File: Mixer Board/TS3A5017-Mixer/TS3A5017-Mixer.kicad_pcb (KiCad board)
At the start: 2 copper layers, 37.8 x 42.9 mm, 10 parts, among them J1 RF-In, J2 CLK0, J3 CLK1, J4 Conn_01x06, U1 TS3A5017RGY

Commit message: Working on mixer board
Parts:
- added C10: .1uf, Capacitor_SMD:C_0201_0603Metric, F.Cu at (107.9, 68.1)
- added C11: .1uf, Capacitor_SMD:C_0201_0603Metric, F.Cu at (110.4, 61.1)
- added C12: .1uf, Capacitor_SMD:C_0201_0603Metric, F.Cu at (110.4, 62.8)
- added C13: .1uf, Capacitor_SMD:C_0201_0603Metric, F.Cu at (110.4, 64.6)
- added C6: .1uf, Capacitor_SMD:C_0201_0603Metric, F.Cu at (107.9, 61.1)
- added C7: .1uf, Capacitor_SMD:C_0201_0603Metric, F.Cu at (107.9, 62.8)
- added C8: .1uf, Capacitor_SMD:C_0201_0603Metric, F.Cu at (107.9, 64.6)
- added C9: .1uf, Capacitor_SMD:C_0201_0603Metric, F.Cu at (107.9, 66.3)
- added R1: 10k, Resistor_SMD:R_0201_0603Metric, F.Cu at (110.4, 66.3)
- added R2: 10k, Resistor_SMD:R_0201_0603Metric, F.Cu at (110.4, 68.1)
- added U2: LMP7715MF, Package_TO_SOT_SMD:SOT-23-5, F.Cu at (109.3, 53.3)
- added U3: LMP7715MF, Package_TO_SOT_SMD:SOT-23-5, F.Cu at (109.3, 58.0)
- J1, J2, J3: footprint Connector_Amphenol:AMPHENOL_901-143-6RFX -> Connector_Coaxial:SMA_Amphenol_901-143_Horizontal
- J4: value Conn_01x06 -> AudioJack4_Ground; footprint Connector_PinHeader_2.54mm:PinHeader_1x06_P2.54mm_Vertical -> Connector_Audio:Jack_3.5mm_CUI_SJ-3523-SMT_Horizontal
- moved J4 56.0 mm to (135.0, 51.4), turned to 0 degrees
- turned J1 to 0 degrees
- turned J2 to -90 degrees
- turned J3 to 90 degrees
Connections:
- C2 pad 1: Net-(J4-Pin_5) -> Net-(U1-1S4)
- C3 pad 1: Net-(J4-Pin_4) -> Net-(U1-1S3)
- C4 pad 1: Net-(J4-Pin_3) -> Net-(U1-1S2)
- C5 pad 1: Net-(J4-Pin_2) -> Net-(U1-1S1)
- U1 pad 10: Net-(J4-Pin_2) -> Net-(U1-1S1)
- U1 pad 11: Net-(J4-Pin_3) -> Net-(U1-1S2)
- U1 pad 12: Net-(J4-Pin_4) -> Net-(U1-1S3)
- U1 pad 13: Net-(J4-Pin_5) -> Net-(U1-1S4)
- U1 pad 3: Net-(J4-Pin_5) -> Net-(U1-1S4)
- U1 pad 4: Net-(J4-Pin_4) -> Net-(U1-1S3)
- U1 pad 5: Net-(J4-Pin_3) -> Net-(U1-1S2)
- U1 pad 6: Net-(J4-Pin_2) -> Net-(U1-1S1)
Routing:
- net Net-(J4-Pin_2): track 53.5 -> 0.00 mm
- net Net-(J4-Pin_3): track 51.6 -> 0.00 mm, vias 1 -> 0
- net Net-(J4-Pin_4): track 47.3 -> 0.00 mm, vias 1 -> 0
- net Net-(J4-Pin_5): track 47.1 -> 0.00 mm, vias 1 -> 0
- net RF-In: track 21.5 -> 0.74 mm
- net /3.3V: track 21.7 -> 2.77 mm
- net GND: track 21.7 -> 7.61 mm, vias 8 -> 6
- net CLK1: track 12.2 -> 0.00 mm, vias 1 -> 0
- net CLK0: track 11.3 -> 0.00 mm, vias 1 -> 0
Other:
- board text removed: "3.3V"
- board text removed: "GND"
- board text removed: "I_Neg"
- board text removed: "I_Pos"
- board text removed: "Q_Neg"
- board text removed: "Q_Pos"

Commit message: Workig on mixer board
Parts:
- C2, C3, C4, C5: footprint Capacitor_SMD:C_1206_3216Metric -> Capacitor_SMD:C_0201_0603Metric
- moved U3 56.9 mm to (150.5, 97.2), turned to 180 degrees
- moved J4 55.6 mm to (133.3, 106.9), turned to 180 degrees
- moved U2 55.2 mm to (142.7, 97.3), turned to 180 degrees
- moved C13 53.7 mm to (150.3, 100.6), turned to 180 degrees
- moved C11 53.7 mm to (152.1, 95.0), turned to 180 degrees
- moved R2 50.8 mm to (150.3, 99.6)
- moved C7 50.5 mm to (142.7, 99.6), turned to 180 degrees
- moved C10 50.3 mm to (148.0, 98.6), turned to 90 degrees
- moved C12 50.3 mm to (149.0, 95.0)
- moved C6 49.3 mm to (140.1, 98.5), turned to 90 degrees
- moved R1 47.1 mm to (142.7, 100.6)
- moved C9 46.2 mm to (144.2, 95.0), turned to 180 degrees
- moved C8 45.1 mm to (141.2, 95.0)
- moved C5 17.4 mm to (141.9, 85.9), turned to 180 degrees
- moved C3 17.0 mm to (152.0, 86.6), turned to 0 degrees
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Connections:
- C11 pad 2: Net-(U3-IN+) -> /I-Pos
- C12 pad 2: Net-(U3-IN-) -> /I-Neg
- C13 pad 2: Net-(U3-IN-) -> /I-Neg
- C2 pad 1: Net-(U1-1S4) -> /I-Neg
- C3 pad 1: Net-(U1-1S3) -> /Q-Neg
- C4 pad 1: Net-(U1-1S2) -> /I-Pos
- C5 pad 1: Net-(U1-1S1) -> /Q-Pos
- C7 pad 2: Net-(U2-IN-) -> /Q-Neg
- C8 pad 2: Net-(U2-IN-) -> /Q-Neg
- C9 pad 2: Net-(U2-IN+) -> /Q-Pos
- R1 pad 1: Net-(U2-IN-) -> /Q-Neg
- R2 pad 1: Net-(U3-IN-) -> /I-Neg
- U1 pad 10: Net-(U1-1S1) -> /Q-Pos
- U1 pad 11: Net-(U1-1S2) -> /I-Pos
- U1 pad 12: Net-(U1-1S3) -> /Q-Neg
- U1 pad 13: Net-(U1-1S4) -> /I-Neg
- U1 pad 3: Net-(U1-1S4) -> /I-Neg
- U1 pad 4: Net-(U1-1S3) -> /Q-Neg
- U1 pad 5: Net-(U1-1S2) -> /I-Pos
- U1 pad 6: Net-(U1-1S1) -> /Q-Pos
- U2 pad 3: Net-(U2-IN+) -> /Q-Pos
- U2 pad 4: Net-(U2-IN-) -> /Q-Neg
- U3 pad 3: Net-(U3-IN+) -> /I-Pos
- U3 pad 4: Net-(U3-IN-) -> /I-Neg
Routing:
- net /I-Neg: track 0.00 -> 32.4 mm, vias 0 -> 3
- net /Q-Neg: track 0.00 -> 29.1 mm, vias 0 -> 3
- net /Q-Pos: track 0.00 -> 21.2 mm, vias 0 -> 3
- net /I-Pos: track 0.00 -> 16.1 mm, vias 0 -> 3
- net RF-In: track 0.74 -> 14.0 mm
- net CLK1: track 0.00 -> 12.2 mm
- net CLK0: track 0.00 -> 11.3 mm
- net GND: track 7.61 -> 17.7 mm, vias 6 -> 22
- net /3.3V: track 2.77 -> 7.68 mm, vias 1 -> 3
- net Net-(U3-OUT): track 0.00 -> 3.16 mm
- net Net-(U2-OUT): track 0.00 -> 2.85 mm
- added copper zone on In2.Cu, net /3.3V
- added copper zone on In1.Cu, net GND
- removed copper zone on B.Cu, net GND
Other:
- copper layers 2 -> 4

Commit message: Working on stuff
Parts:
- added C14: 1uf, Capacitor_SMD:C_0201_0603Metric, F.Cu at (157.4, 98.3)
- added C15: 1uf, Capacitor_SMD:C_0201_0603Metric, F.Cu at (153.2, 103.6)
- added J5: PJ-320D-A, Connector_Audio:HRO_PJ-320D-A, F.Cu at (159.3, 108.8)
- J4: value AudioJack4_Ground -> Conn_01x02_Pin; footprint Connector_Audio:Jack_3.5mm_CUI_SJ-3523-SMT_Horizontal -> Connector_PinHeader_2.54mm:PinHeader_1x02_P2.54mm_Vertical
- moved J4 2.90 mm to (132.6, 104.1), turned to 0 degrees
- moved C3 2.11 mm to (153.4, 88.1)
- moved C5 1.92 mm to (143.4, 84.7)
- moved C2 1.59 mm to (152.4, 89.2)
- moved J3 1.53 mm to (131.8, 89.9)
- moved J1 1.09 mm to (146.5, 78.2)
- moved J2 1.08 mm to (160.6, 89.9)
- moved C4 0.93 mm to (142.4, 85.9)
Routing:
- net Net-(C14-Pad1): track 0.00 -> 13.1 mm
- net /Q-Neg: track 29.1 -> 41.1 mm
- net Net-(U2-OUT): track 2.85 -> 14.2 mm
- net /I-Pos: track 16.1 -> 27.1 mm
- net GND: track 17.7 -> 27.4 mm, vias 22 -> 17
- net /Q-Pos: track 21.2 -> 30.1 mm
- net Net-(U3-OUT): track 3.16 -> 8.33 mm
- net /I-Neg: track 32.4 -> 36.0 mm
- net Net-(C15-Pad2): track 0.00 -> 2.61 mm
- net CLK1: track 12.2 -> 13.7 mm
- net RF-In: track 14.0 -> 15.4 mm
- net CLK0: track 11.3 -> 12.3 mm
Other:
- board text added: "3.3V"
- board text added: "CLK0"
- board text added: "CLK1"
- board text added: "GND"
- board text added: "RF-IN"
- board text added: "v0.2 Tayloe Mixer + Amp 04/04/24 Eric Dynowski"

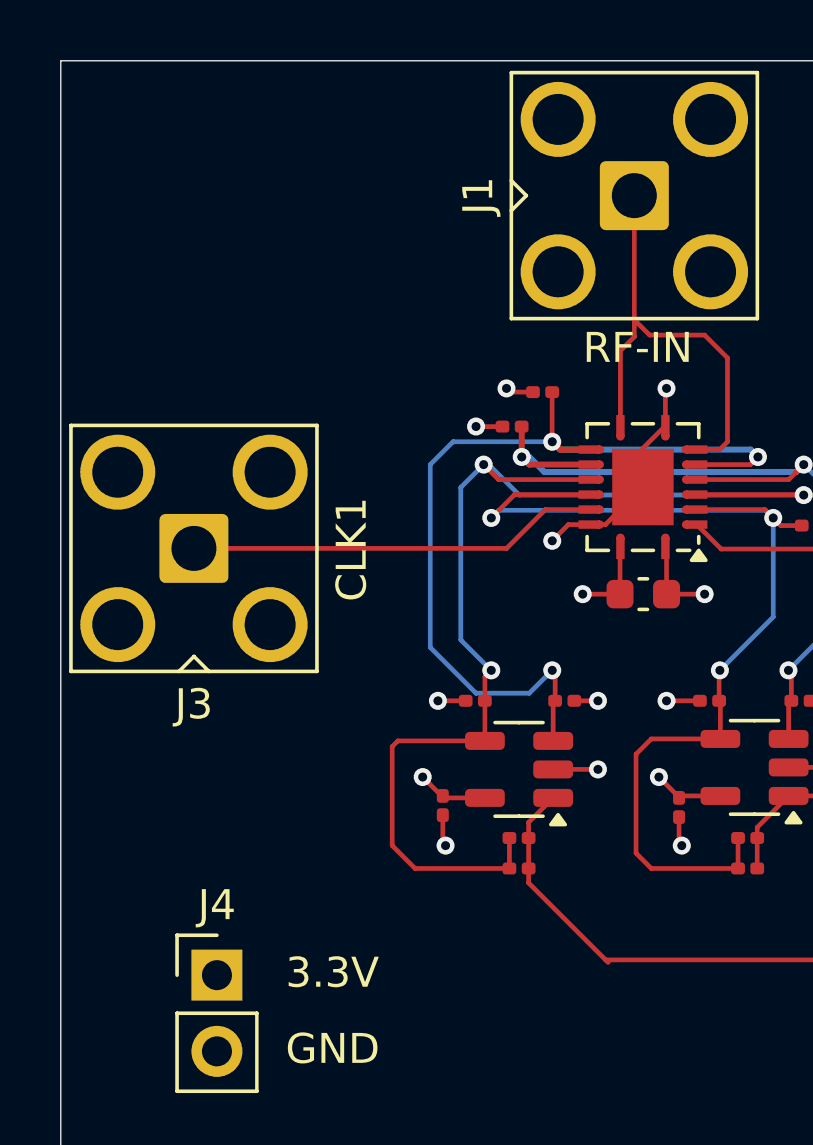
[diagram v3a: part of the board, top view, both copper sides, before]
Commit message: Working on silkscreen and ordering
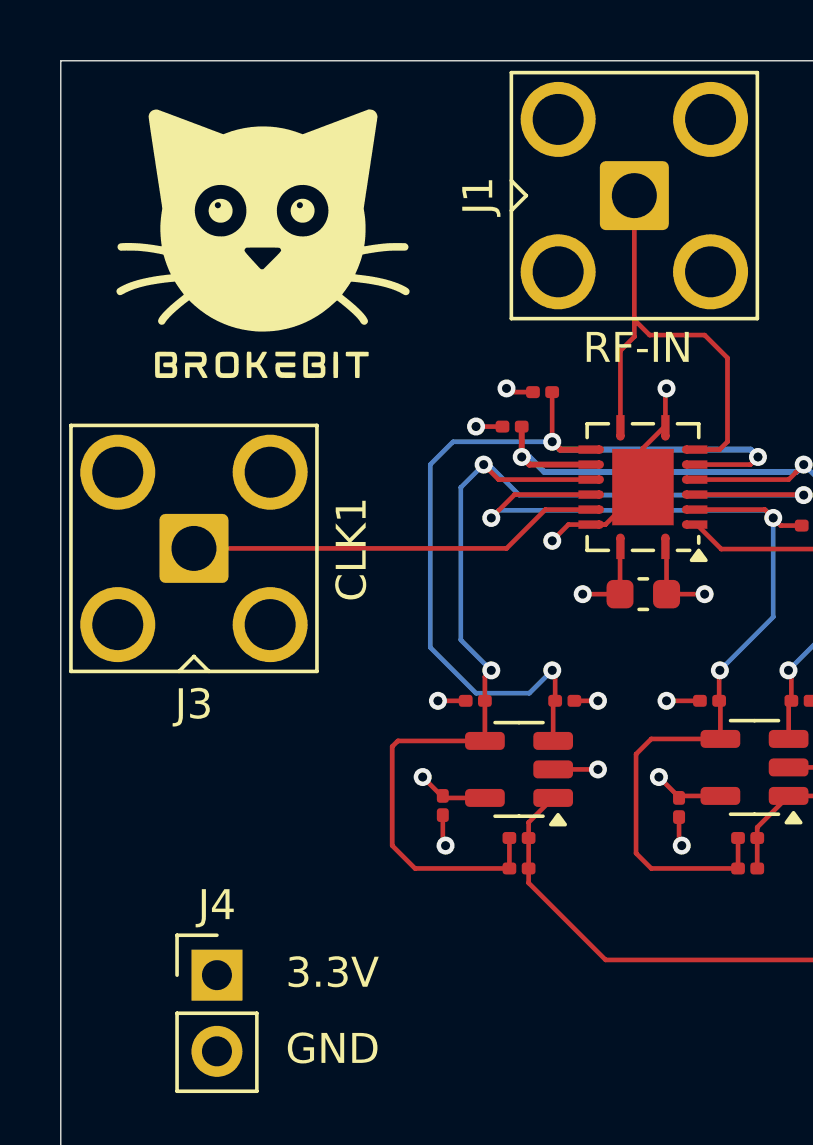
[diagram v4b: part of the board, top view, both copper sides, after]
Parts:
- added G***: LOGO, LOGO, F.Cu at (134.1, 79.8)

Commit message: Fixing things
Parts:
- C1: footprint Capacitor_SMD:C_0603_1608Metric -> Capacitor_SMD:C_0201_0603Metric
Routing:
- net /3.3V: track 7.51 -> 8.17 mm
- net GND: track 27.4 -> 28.0 mm
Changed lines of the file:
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@@
 		)
 	)
-	(footprint "Capacitor_SMD:C_0603_1608Metric"
+	(footprint "Capacitor_SMD:C_0201_0603Metric"
 		(layer "F.Cu")
 		(at 146.799 91.44)
-		(descr "Capacitor SMD 0603 (1608 Metric), square (rectangular) end terminal, IPC_7351 nominal, (Body size source: IPC-SM-782 page 76, https://www.pcb-3d.com/wordpress/wp-content/uploads/ipc-sm-782a_amendment_1_and_2.pdf), generated with kicad-footprint-generator")
+		(descr "Capacitor SMD 0201 (0603 Metric), square (rectangular) end terminal, IPC_7351 nominal, (Body size source: https://www.vishay.com/docs/20052/crcw0201e3.pdf), generated with kicad-footprint-generator")
 		(tags "capacitor")
 		(property "Reference" "C1"
-			(at -2.54 0 0)
+			(at 0 -1.05 0)
 			(layer "F.SilkS")
 			(hide yes)
@@
 		)
 		(property "Value" ".1uf"
-			(at 0 1.43 0)
+			(at 0 1.05 0)
 			(layer "F.Fab")
 			(hide yes)
@@
 			)
 		)
-		(property "Footprint" "Capacitor_SMD:C_0603_1608Metric"
+		(property "Footprint" "Capacitor_SMD:C_0201_0603Metric"
 			(at 0 0 0)
 			(unlocked yes)
@@
 		(attr smd)
 		(fp_line
-			(start -0.14058 -0.51)
-			(end 0.14058 -0.51)
-			(stroke
-				(width 0.12)
-				(type solid)
-			)
-			(layer "F.SilkS")
-		)
-		(fp_line
-			(start -0.14058 0.51)
-			(end 0.14058 0.51)
-			(stroke
-				(width 0.12)
-				(type solid)
-			)
-			(layer "F.SilkS")
-		)
-		(fp_line
-			(start -1.48 -0.73)
-			(end 1.48 -0.73)
+			(start -0.7 -0.35)
+			(end 0.7 -0.35)
 			(stroke
 				(width 0.05)
@@
 		)
 		(fp_line
-			(start -1.48 0.73)
-			(end -1.48 -0.73)
+			(start -0.7 0.35)
+			(end -0.7 -0.35)
 			(stroke
 				(width 0.05)
@@
 		)
 		(fp_line
-			(start 1.48 -0.73)
-			(end 1.48 0.73)
+			(start 0.7 -0.35)
+			(end 0.7 0.35)
 			(stroke
 				(width 0.05)
@@
 		)
 		(fp_line
-			(start 1.48 0.73)
-			(end -1.48 0.73)
+			(start 0.7 0.35)
+			(end -0.7 0.35)
 			(stroke
 				(width 0.05)
@@
 		)
 		(fp_line
-			(start -0.8 -0.4)
-			(end 0.8 -0.4)
+			(start -0.3 -0.15)
+			(end 0.3 -0.15)
 			(stroke
 				(width 0.1)
@@
 		)
 		(fp_line
-			(start -0.8 0.4)
-			(end -0.8 -0.4)
+			(start -0.3 0.15)
+			(end -0.3 -0.15)
 			(stroke
 				(width 0.1)
@@
 		)
 		(fp_line
-			(start 0.8 -0.4)
-			(end 0.8 0.4)
+			(start 0.3 -0.15)
+			(end 0.3 0.15)
 			(stroke
 				(width 0.1)
@@
 		)
 		(fp_line
-			(start 0.8 0.4)
-			(end -0.8 0.4)
+			(start 0.3 0.15)
+			(end -0.3 0.15)
 			(stroke
 				(width 0.1)
@@
 		)
 		(fp_text user "${REFERENCE}"
-			(at 0.013 1.016 0)
+			(at 0 -0.68 0)
 			(layer "F.Fab")
 			(effects
 				(font
-					(size 0.4 0.4)
-					(thickness 0.06)
+					(size 0.25 0.25)
+					(thickness 0.04)
 				)
 			)
 		)
+		(pad "" smd roundrect
+			(at -0.345 0)
+			(size 0.318 0.36)
+			(layers "F.Paste")
+			(roundrect_rratio 0.25)
+		)
+		(pad "" smd roundrect
+			(at 0.345 0)
+			(size 0.318 0.36)
+			(layers "F.Paste")
+			(roundrect_rratio 0.25)
+		)
 		(pad "1" smd roundrect
-			(at -0.775 0)
-			(size 0.9 0.95)
-			(layers "F.Cu" "F.Paste" "F.Mask")
+			(at -0.32 0)
+			(size 0.46 0.4)
+			(layers "F.Cu" "F.Mask")
 			(roundrect_rratio 0.25)
 			(net 1 "/3.3V")
@@
 		)
 		(pad "2" smd roundrect
-			(at 0.775 0)
-			(size 0.9 0.95)
-			(layers "F.Cu" "F.Paste" "F.Mask")
+			(at 0.32 0)
+			(size 0.46 0.4)
+			(layers "F.Cu" "F.Mask")
 			(roundrect_rratio 0.25)
 			(net 2 "GND")
 			(pintype "passive")
 		)
-		(model "${KICAD8_3DMODEL_DIR}/Capacitor_SMD.3dshapes/C_0603_1608Metric.wrl"
+		(model "${KICAD8_3DMODEL_DIR}/Capacitor_SMD.3dshapes/C_0201_0603Metric.wrl"
 			(offset
 				(xyz 0 0 0)
@@
 	)
 	(segment
-		(start 146.024 91.44)
+		(start 146.479 91.44)
 		(end 144.78 91.44)
 		(width 0.156464)
@@
 	)
 	(segment
-		(start 146.024 91.44)
-		(end 146.024 89.929)
-		(width 0.156464)
-		(layer "F.Cu")
-		(net 1)
-	)
-	(segment
 		(start 141.5195 98.232)
 		(end 140.183 98.232)
@@
 	)
 	(segment
+		(start 146.037 89.916)
+		(end 146.304 90.183)
+		(width 0.156464)
+		(layer "F.Cu")
+		(net 1)
+	)
+	(segment
+		(start 146.304 90.678)
+		(end 146.479 90.853)
+		(width 0.156464)
+		(layer "F.Cu")
+		(net 1)
+	)
+	(segment
 		(start 149.369 98.166)
 		(end 148.057 98.166)
@@
 	)
 	(segment
+		(start 146.479 90.853)
+		(end 146.479 91.44)
+		(width 0.156464)
+		(layer "F.Cu")
+		(net 1)
+	)
+	(segment
 		(start 140.117 98.166)
 		(end 140.076 98.166)
@@
 	)
 	(segment
+		(start 146.304 90.183)
+		(end 146.304 90.678)
+		(width 0.156464)
+		(layer "F.Cu")
+		(net 1)
+	)
+	(segment
 		(start 147.991 98.232)
 		(end 147.991 98.207)
@@
 	)
 	(segment
-		(start 147.574 91.44)
-		(end 147.574 89.953)
-		(width 0.156464)
-		(layer "F.Cu")
-		(net 2)
-	)
-	(segment
 		(start 140.879 94.996)
 		(end 139.954 94.996)
@@
 	)
 	(segment
-		(start 147.574 91.44)
-		(end 148.844 91.44)
+		(start 147.574 89.953)
+		(end 147.574 90.17)
 		(width 0.156464)
 		(layer "F.Cu")
@@
 	)
 	(segment
+		(start 147.119 90.879)
+		(end 147.119 91.44)
+		(width 0.156464)
+		(layer "F.Cu")
+		(net 2)
+	)
+	(segment
 		(start 162.56 102.616)
 		(end 162.56 100.584)
@@
 	)
 	(segment
+		(start 147.119 91.44)
+		(end 148.844 91.44)
+		(width 0.156464)
+		(layer "F.Cu")
+		(net 2)
+	)
+	(segment
 		(start 140.117 99.731)
 		(end 140.208 99.822)
@@
 	)
 	(segment
+		(start 147.32 90.678)
+		(end 147.119 90.879)
+		(width 0.156464)
+		(layer "F.Cu")
+		(net 2)
+	)
+	(segment
+		(start 147.32 90.424)
+		(end 147.32 90.678)
+		(width 0.156464)
+		(layer "F.Cu")
+		(net 2)
+	)
+	(segment
 		(start 144.992 89.121)
 		(end 144.305 89.121)
@@
 		(width 0.156464)
 		(layer "F.Cu")
+		(net 2)
+	)
+	(segment
+		(start 147.574 90.17)
+		(end 147.32 90.424)
+		(width 0.156464)
+		(layer "F.Cu")
